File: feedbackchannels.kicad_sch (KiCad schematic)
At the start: 35 parts

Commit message: Progress on feedback channels
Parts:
- added C?: 10uF, Capacitor_SMD:C_0603_1608Metric, symbol Device:C_Small
- added C? (x2): 1uF, Capacitor_SMD:C_0603_1608Metric, symbol Device:C_Small
- added C?: 0.1uF, Capacitor_SMD:C_0603_1608Metric, symbol Device:C_Small
- added U? (x3): TLV7031, Package_TO_SOT_SMD:SOT-353_SC-70-5, symbol actuation:TLV7031
- added U?: TPS709, Package_TO_SOT_SMD:SOT-23-5, symbol actuation:TPS709
- J?: value FB CH1 -> FB CH6
- J?: value FB CH1 -> FB CH2
- J?: value FB CH1 -> FB CH7
- J?: value FB CH1 -> FB CH4
- J?: value FB CH1 -> FB CH8
- J?: value FB CH1 -> FB CH3
- J?: value FB CH1 -> FB CH5
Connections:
- net +3.3V: no longer J?.1 (Pin_1), J?.1 (Pin_1), J?.1 (Pin_1), J?.1 (Pin_1), J?.1 (Pin_1), J?.1 (Pin_1), J?.1 (Pin_1), J?.1 (Pin_1)
- net GND: now also C?.2, C?.2; no longer U?.3, U?.3, U?.3, U?.3, U?.3, U?.3, U?.3, U?.3
- new net 3.3V_PWR: C?.1, C?.1, J?.1 (Pin_1), J?.1 (Pin_1), J?.1 (Pin_1), J?.1 (Pin_1), J?.1 (Pin_1), J?.1 (Pin_1), J?.1 (Pin_1), U?.5 (OUT)
- new net GNDPWR: C?.2, C?.2, U?.2 (GND), U?.3, U?.3, U?.3, U?.3, U?.3, U?.3, U?.3, U?.3
- new net VBUS: C?.1, C?.1, U?.1 (IN), U?.3 (EN)
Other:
- moved on the sheet: C?, J?, R?, U?
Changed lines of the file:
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@@
 (kicad_sch (version 20211123) (generator eeschema)
-  (paper "User" 200 350.012)
+  (paper "User" 299.999 299.999)

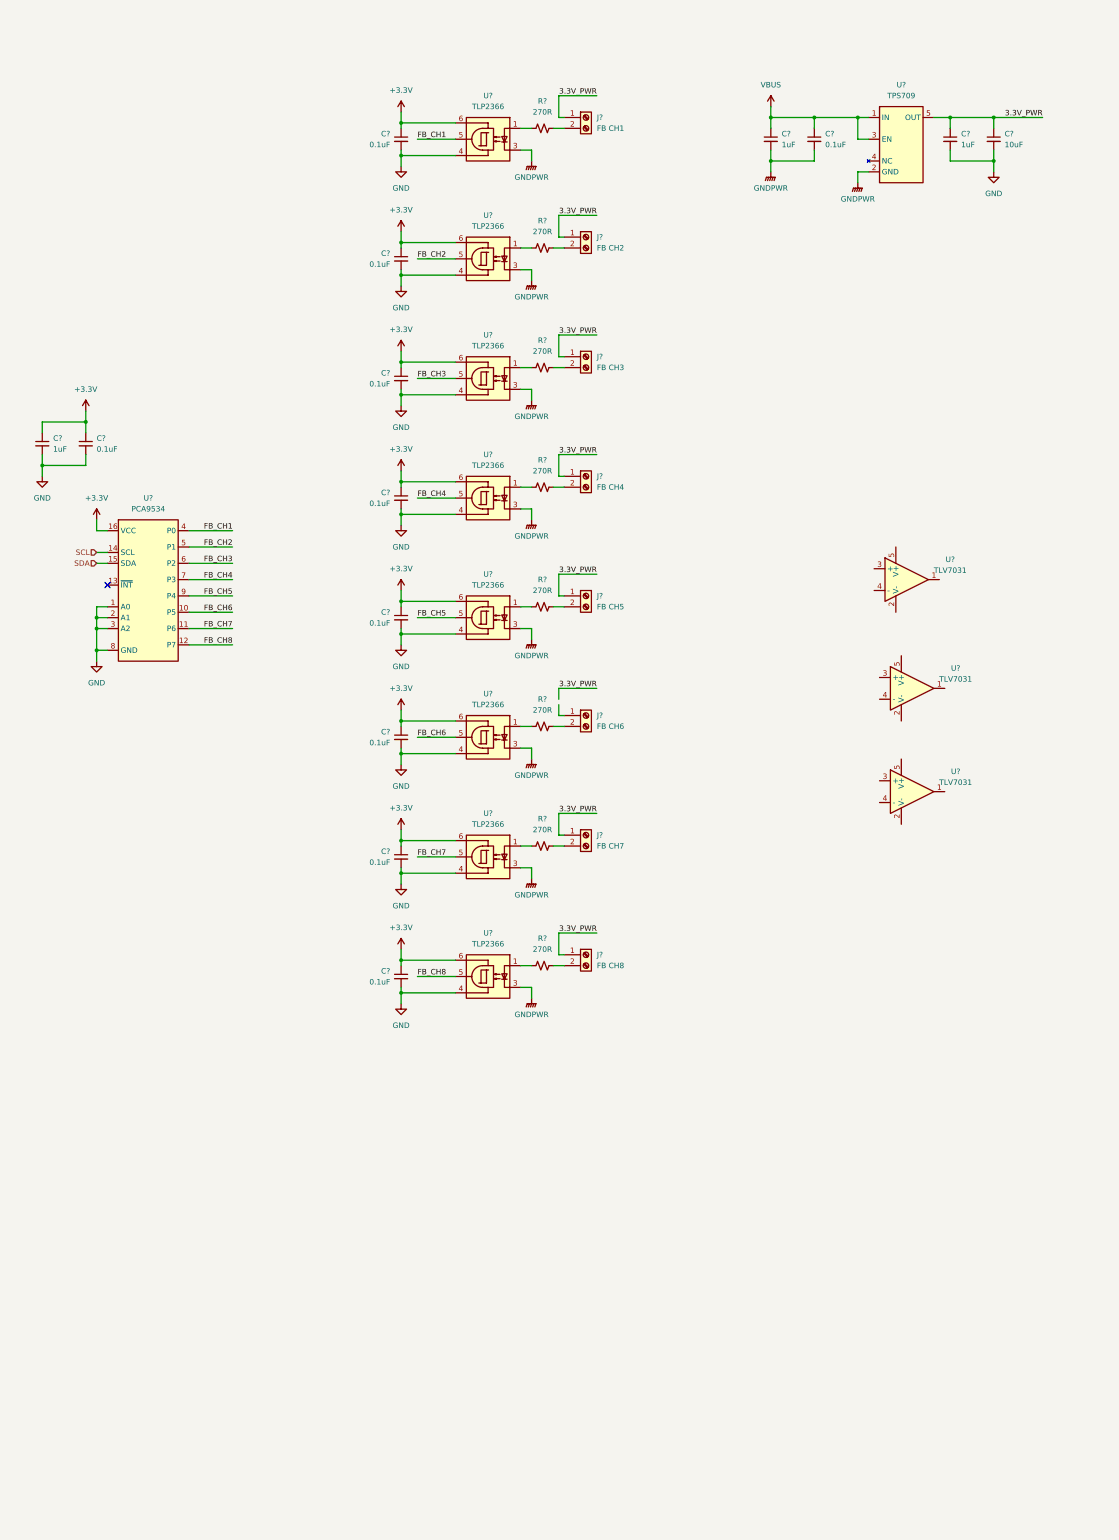
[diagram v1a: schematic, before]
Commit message: Voltage threshold detection feedback channels
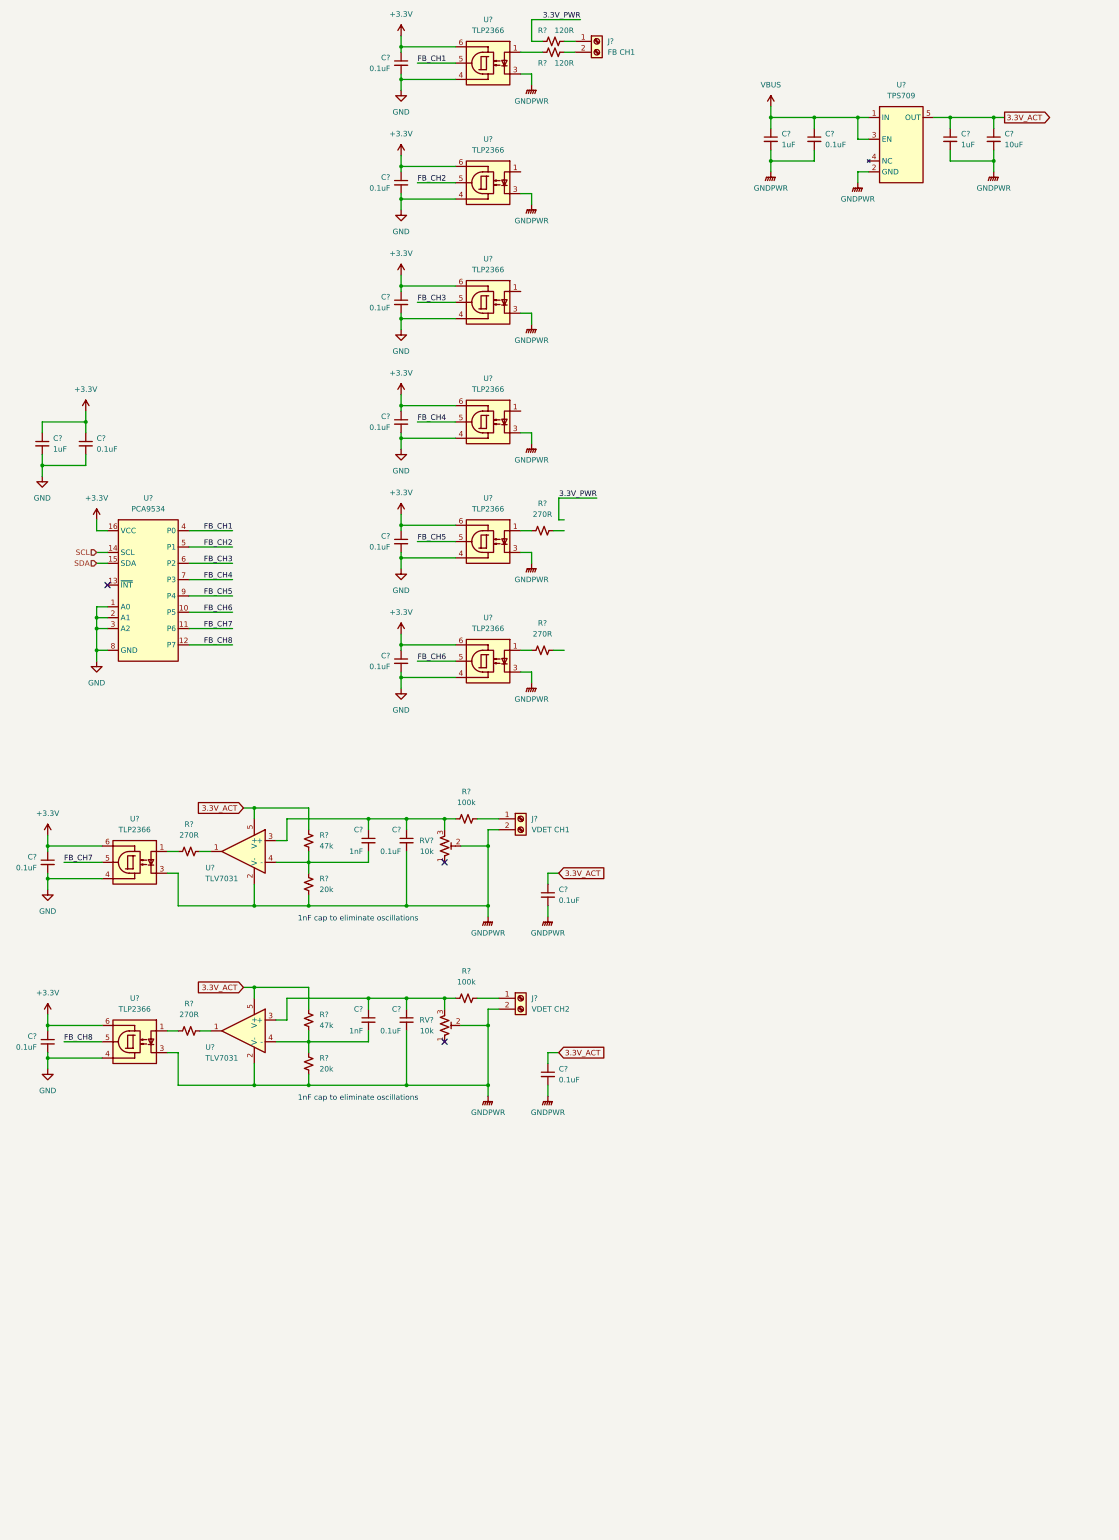
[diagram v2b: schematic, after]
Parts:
- removed C?: 0.1uF, Capacitor_SMD:C_0603_1608Metric, symbol Device:C_Small
- removed J?: FB CH1, symbol Connector:Screw_Terminal_01x02
- removed J?: FB CH6, symbol Connector:Screw_Terminal_01x02
- removed J?: FB CH2, symbol Connector:Screw_Terminal_01x02
- removed J?: FB CH7, symbol Connector:Screw_Terminal_01x02
- removed J?: FB CH4, symbol Connector:Screw_Terminal_01x02
- removed J?: FB CH8, symbol Connector:Screw_Terminal_01x02
- removed J?: FB CH3, symbol Connector:Screw_Terminal_01x02
- removed J?: FB CH5, symbol Connector:Screw_Terminal_01x02
- removed R? (x4): 270R, symbol Device:R_Small_US
- removed U? (x2): TLV7031, Package_TO_SOT_SMD:SOT-353_SC-70-5, symbol actuation:TLV7031
- removed U?: TLP2366, actuation:TLP2366, symbol actuation:TLP2366
- added C? (x2): 1nF, symbol Device:C_Small
- added C? (x4): 0.1uF, symbol Device:C_Small
- added C?: 0.1uF, Capacitor_SMD:C_0603_1608Metric, symbol Device:C_Small
- added J?: FB CH1, TerminalBlock_Phoenix:TerminalBlock_Phoenix_PT-1,5-2-5.0-H_1x02_P5.00mm_Horizontal, symbol Connector:Screw_Terminal_01x02
- added J?: VDET CH2, symbol Connector:Screw_Terminal_01x02
- added J?: VDET CH1, symbol Connector:Screw_Terminal_01x02
- added R? (x2): 47k, symbol Device:R_Small_US
- added R? (x2): 20k, symbol Device:R_Small_US
- added R?: 120R, symbol Device:R_Small_US
- added R?: 270R, symbol Device:R_Small_US
- added R? (x2): 100k, symbol Device:R_Small_US
- added RV? (x2): 10k, symbol Device:R_Potentiometer_Trim_US
- added U?: TLV7031, Package_TO_SOT_SMD:SOT-353_SC-70-5, symbol actuation:TLV7031
- added U?: TLP2366, actuation:TLP2366, symbol actuation:TLP2366
- R?: value 270R -> 120R
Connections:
- net +3.3V: now also C?.1, U?.6
- net 3.3V_PWR: now also R?.2; no longer C?.1, C?.1, U?.5 (OUT)
- net FB_CH8: now also U?.5
- net GND: now also C?.2, U?.4; no longer C?.2, C?.2
- net GNDPWR: now also C?.2, C?.2, U?.2 (V-), C?.2, C?.2, C?.2, C?.2, J?.2 (Pin_2), J?.2 (Pin_2), R?.2, R?.2, RV?.2, RV?.2, U?.2 (V-), U?.3
- net at R?.2: now also J?.2 (Pin_2)
- net at R?.2: now also U?.1
- net at U?.3 (+): now also C?.1, C?.1, R?.1, RV?.3
- net at U?.4 (-): now also C?.2, R?.1, R?.2
- net 3.3V_ACT: now reaches U?.5 (V+)
- net 3.3V_ACT: now also C?.1, C?.1, U?.5 (OUT), C?.1, C?.1, R?.1, R?.1, U?.5 (V+)
- new net: C?.1, C?.1, R?.1, RV?.3, U?.3 (+)
- new net: C?.2, R?.1, R?.2, U?.4 (-)
- new net: J?.1 (Pin_1), R?.1
- new net: R?.2, U?.1
- new net: J?.1 (Pin_1), R?.2 (x2)
- new net: R?.1, U?.1
- no-connect marks 1 -> 3
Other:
- note added: "1nF cap to eliminate oscillations"
- moved on the sheet: C?, R?, U?

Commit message: Feedback channels and status LEDs
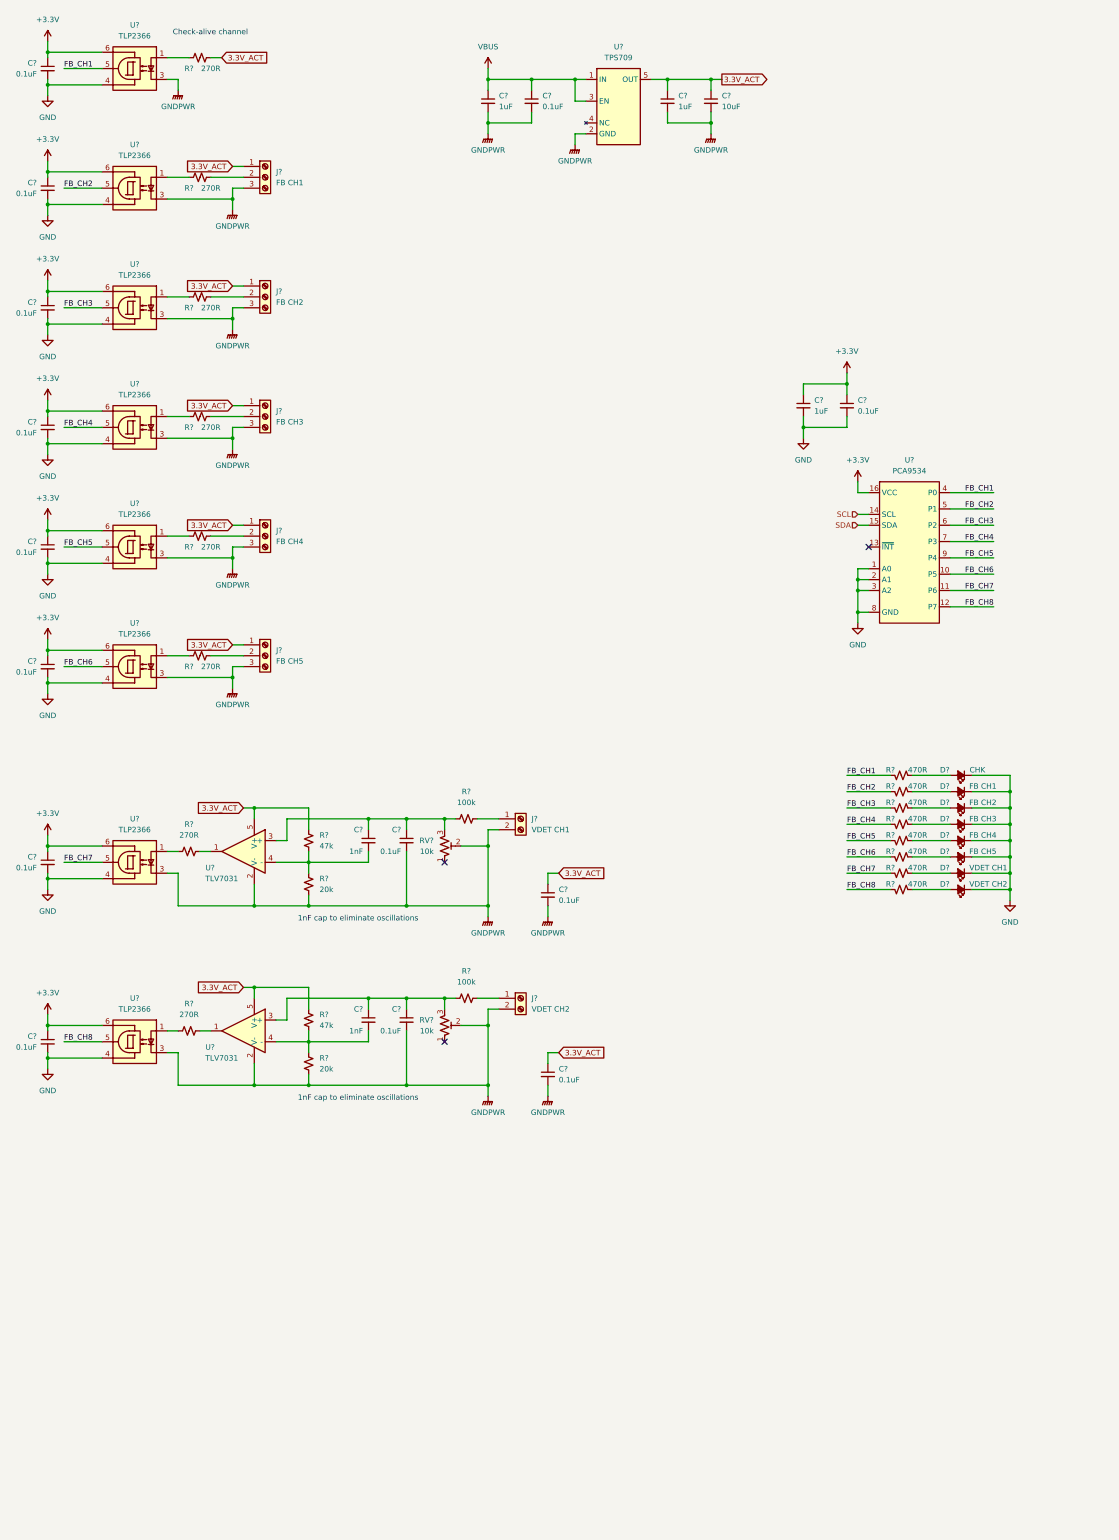
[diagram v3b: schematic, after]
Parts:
- removed J?: FB CH1, TerminalBlock_Phoenix:TerminalBlock_Phoenix_PT-1,5-2-5.0-H_1x02_P5.00mm_Horizontal, symbol Connector:Screw_Terminal_01x02
- removed R?: 120R, symbol Device:R_Small_US
- removed R? (x2): 270R, symbol Device:R_Small_US
- added D?: VDET CH2, symbol Device:LED_Small_Filled
- added D?: FB CH1, symbol Device:LED_Small_Filled
- added D?: FB CH5, symbol Device:LED_Small_Filled
- added D?: CHK, symbol Device:LED_Small_Filled
- added D?: VDET CH1, symbol Device:LED_Small_Filled
- added D?: FB CH3, symbol Device:LED_Small_Filled
- added D?: FB CH2, symbol Device:LED_Small_Filled
- added D?: FB CH4, symbol Device:LED_Small_Filled
- added J?: FB CH3, symbol Connector:Screw_Terminal_01x03
- added J?: FB CH2, symbol Connector:Screw_Terminal_01x03
- added J?: FB CH4, symbol Connector:Screw_Terminal_01x03
- added J?: FB CH5, symbol Connector:Screw_Terminal_01x03
- added J?: FB CH1, symbol Connector:Screw_Terminal_01x03
- added R? (x8): 470R, symbol Device:R_Small_US
- added R? (x5): 270R, symbol Device:R_Small_US
- R?: value 120R -> 270R
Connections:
- net 3.3V_ACT: now also R?.2, J?.1 (Pin_1), J?.1 (Pin_1), J?.1 (Pin_1), J?.1 (Pin_1), J?.1 (Pin_1)
- net FB_CH1: now also R?.1
- net FB_CH2: now also R?.1
- net FB_CH3: now also R?.1
- net FB_CH4: now also R?.1
- net FB_CH5: now also R?.1
- net FB_CH6: now also R?.1
- net FB_CH7: now also R?.1
- net FB_CH8: now also R?.1
- net GND: now also D?.1 (K), D?.1 (K), D?.1 (K), D?.1 (K), D?.1 (K), D?.1 (K), D?.1 (K), D?.1 (K)
- net GNDPWR: now also J?.3 (Pin_3), J?.3 (Pin_3), J?.3 (Pin_3), J?.3 (Pin_3), J?.3 (Pin_3)
- net at U?.1: now also R?.1 (x5)
- new net: D?.2 (A), R?.2 (x8)
- new net: J?.2 (Pin_2), R?.2 (x5)
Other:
- note added: "Check-alive channel"
- moved on the sheet: C?, R?, U?

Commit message: Check-safe channel with buffer
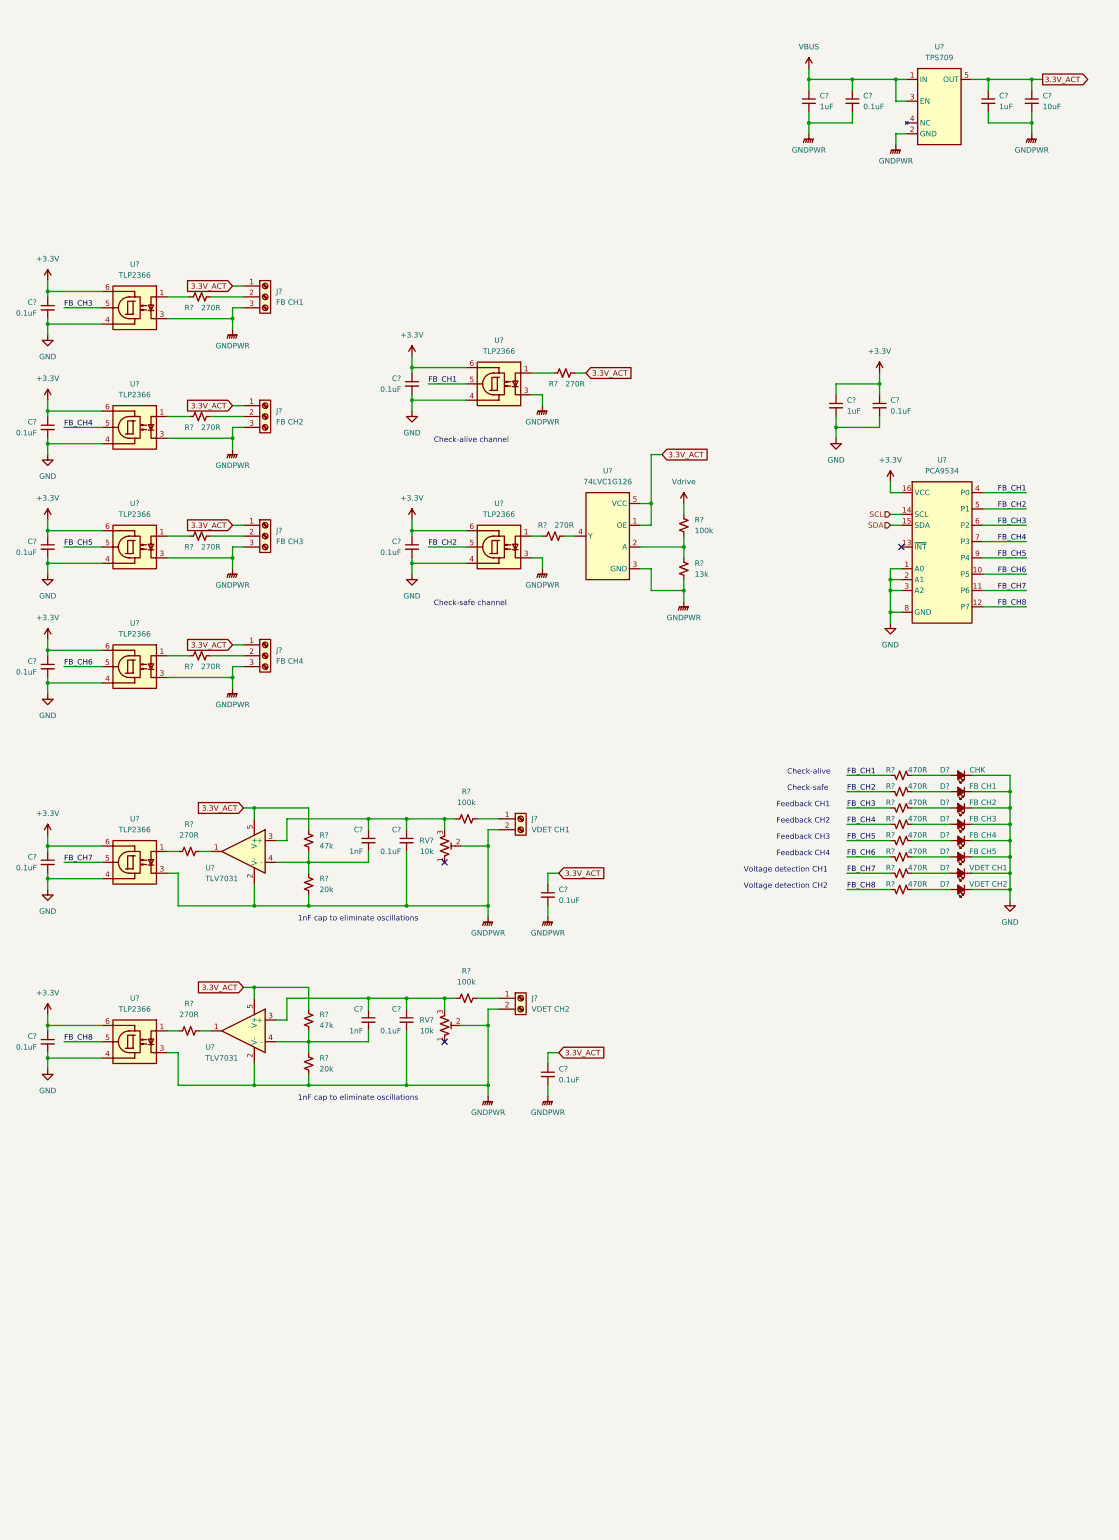
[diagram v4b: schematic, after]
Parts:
- removed J?: FB CH1, symbol Connector:Screw_Terminal_01x03
- added R?: 100k, symbol Device:R_Small_US
- added R?: 13k, symbol Device:R_Small_US
- added U?: 74LVC1G126, Package_TO_SOT_SMD:SOT-23-5, symbol actuation:74LVC1G126
- J?: value FB CH3 -> FB CH2
- J?: value FB CH2 -> FB CH1
- J?: value FB CH4 -> FB CH3
- J?: value FB CH5 -> FB CH4
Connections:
- net 3.3V_ACT: now also U?.1 (OE), U?.5 (VCC)
- net GNDPWR: now also R?.2, U?.3 (GND)
- net at U?.1: now also R?.2; no longer R?.1
- new net: R?.1, R?.2, U?.2 (A)
- new net: R?.1, U?.4 (Y)
- new net Vdrive: R?.1
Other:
- note added: "Check-alive"
- note added: "Check-safe"
- note added: "Check-safe channel"
- note added: "Feedback CH1"
- note added: "Feedback CH2"
- note added: "Feedback CH3"
- note added: "Feedback CH4"
- note added: "Voltage detection CH1"
- note added: "Voltage detection CH2"
- moved on the sheet: C?, R?, U?

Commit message: Preliminary power scheme
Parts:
- added D?: FB PWR, symbol Device:LED_Small_Filled
- added R?: 470R, symbol Device:R_Small_US
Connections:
- net 3.3V_ACT: now also D?.2 (A)
- net GND: now also R?.2
- new net: D?.1 (K), R?.1
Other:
- moved on the sheet: C?, D?, J?, R?, U?
